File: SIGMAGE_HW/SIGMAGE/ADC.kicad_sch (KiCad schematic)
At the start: 34 parts, among them J2 SJ63073E, J3 SJ63073E, J4 SJ63073E, J5 SJ63073E, J7 TSW10607GS, J8 TSW10607GS, U4 OPA1612AIDRGR, U5 PCM1803ADB, U6 OPA1612AIDRGR, U7 PCM1803ADB

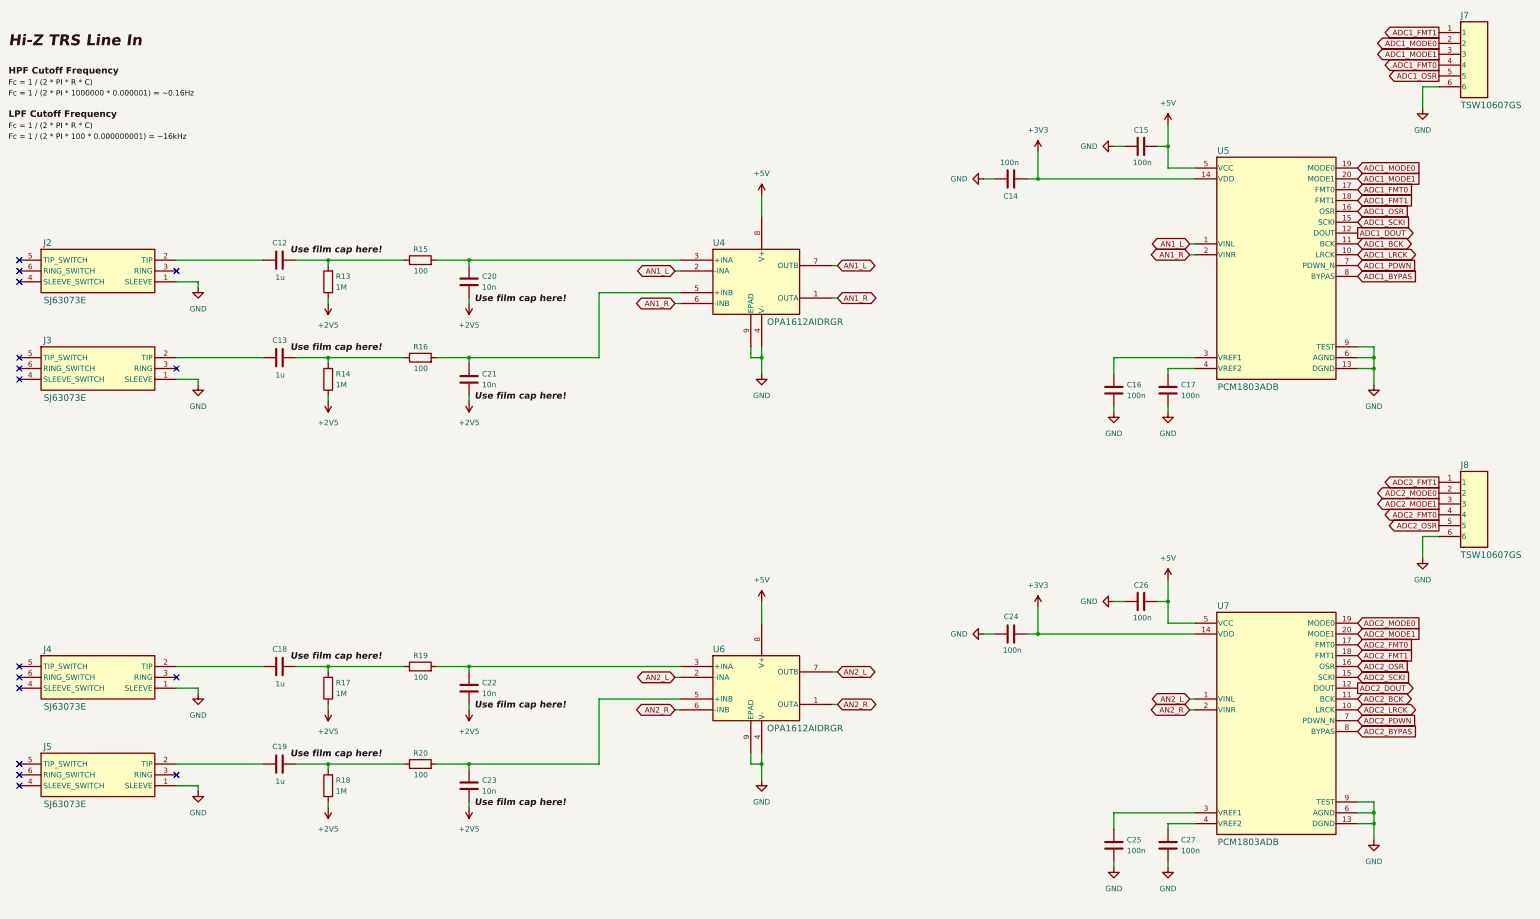
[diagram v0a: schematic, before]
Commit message: Adding a view DAC's
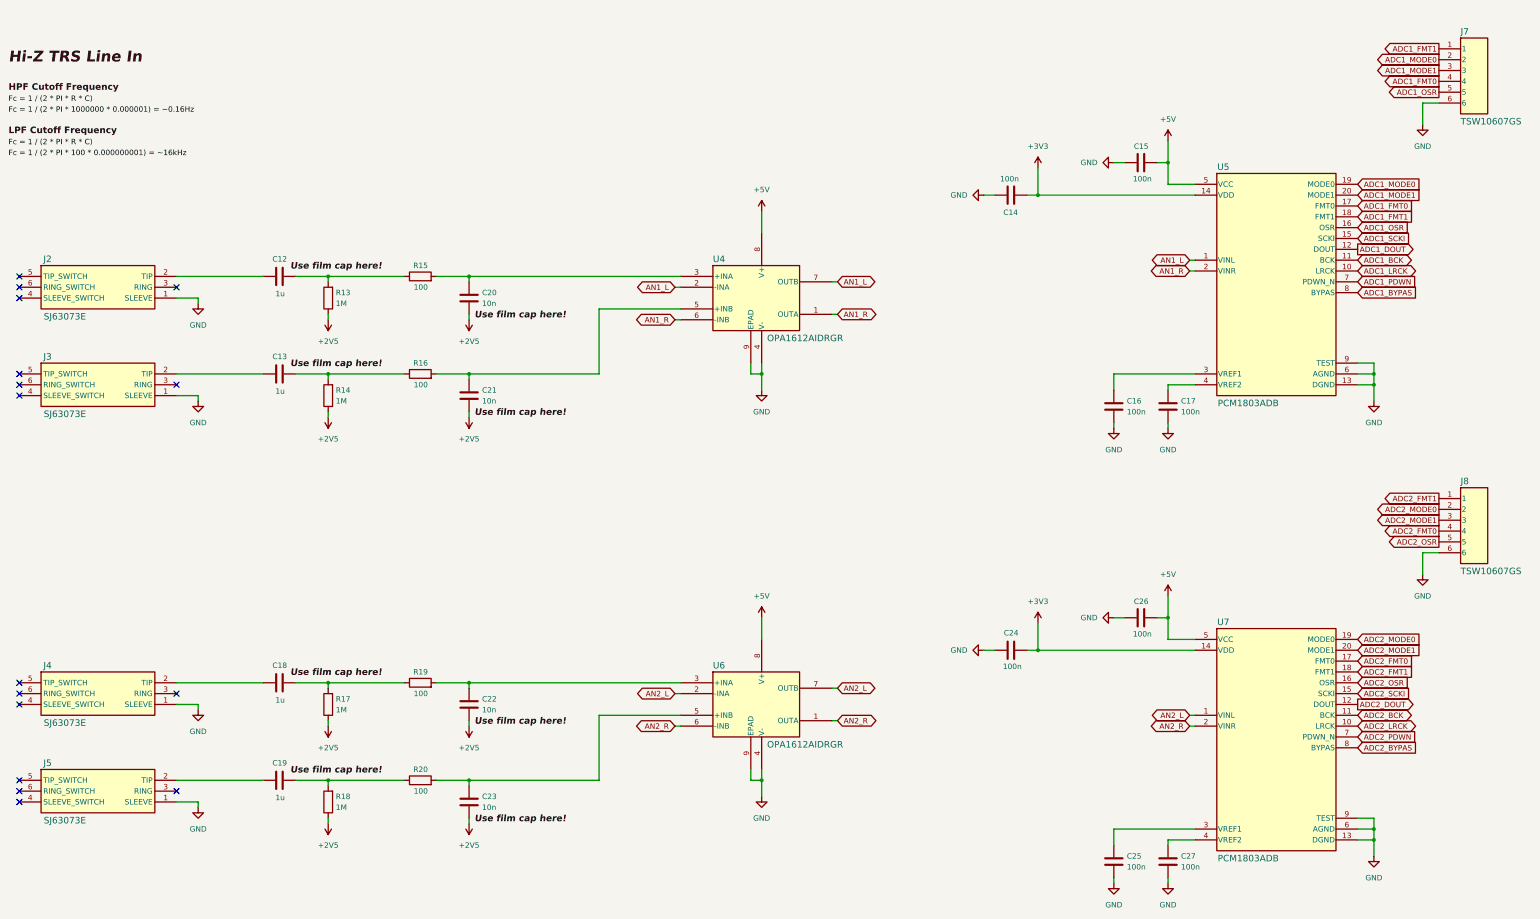
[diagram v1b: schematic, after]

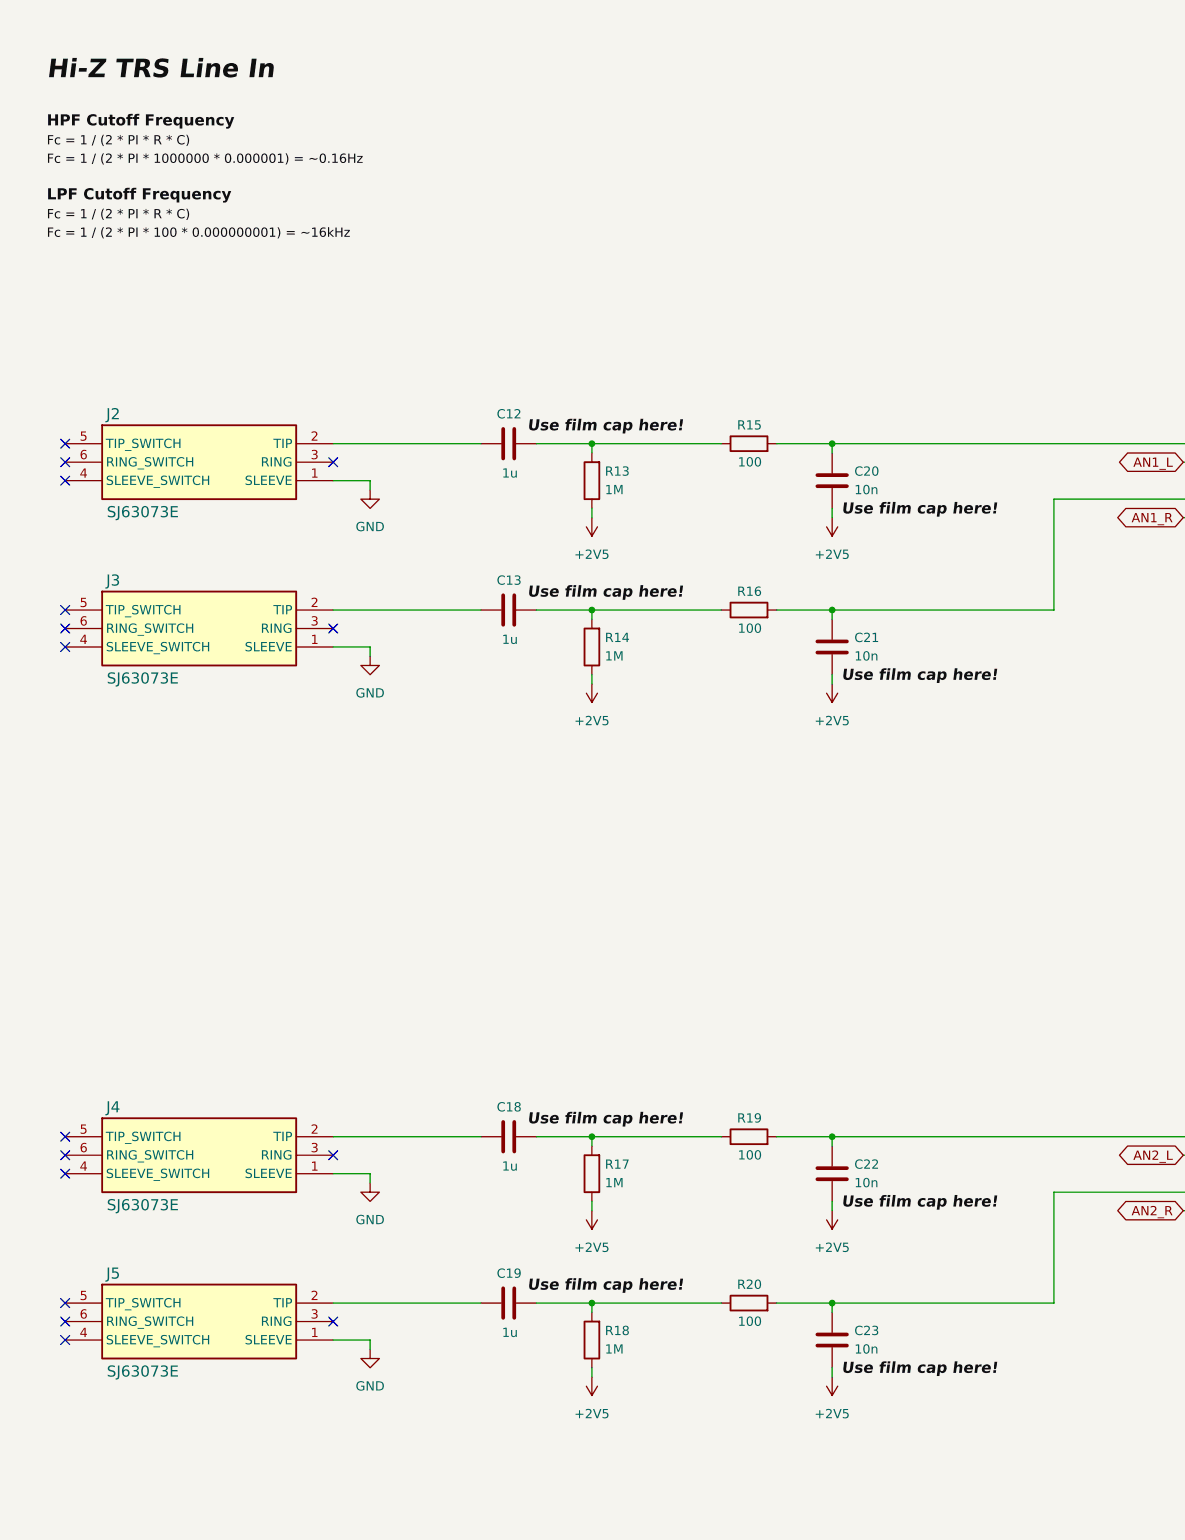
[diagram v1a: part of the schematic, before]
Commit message: More DAC changes
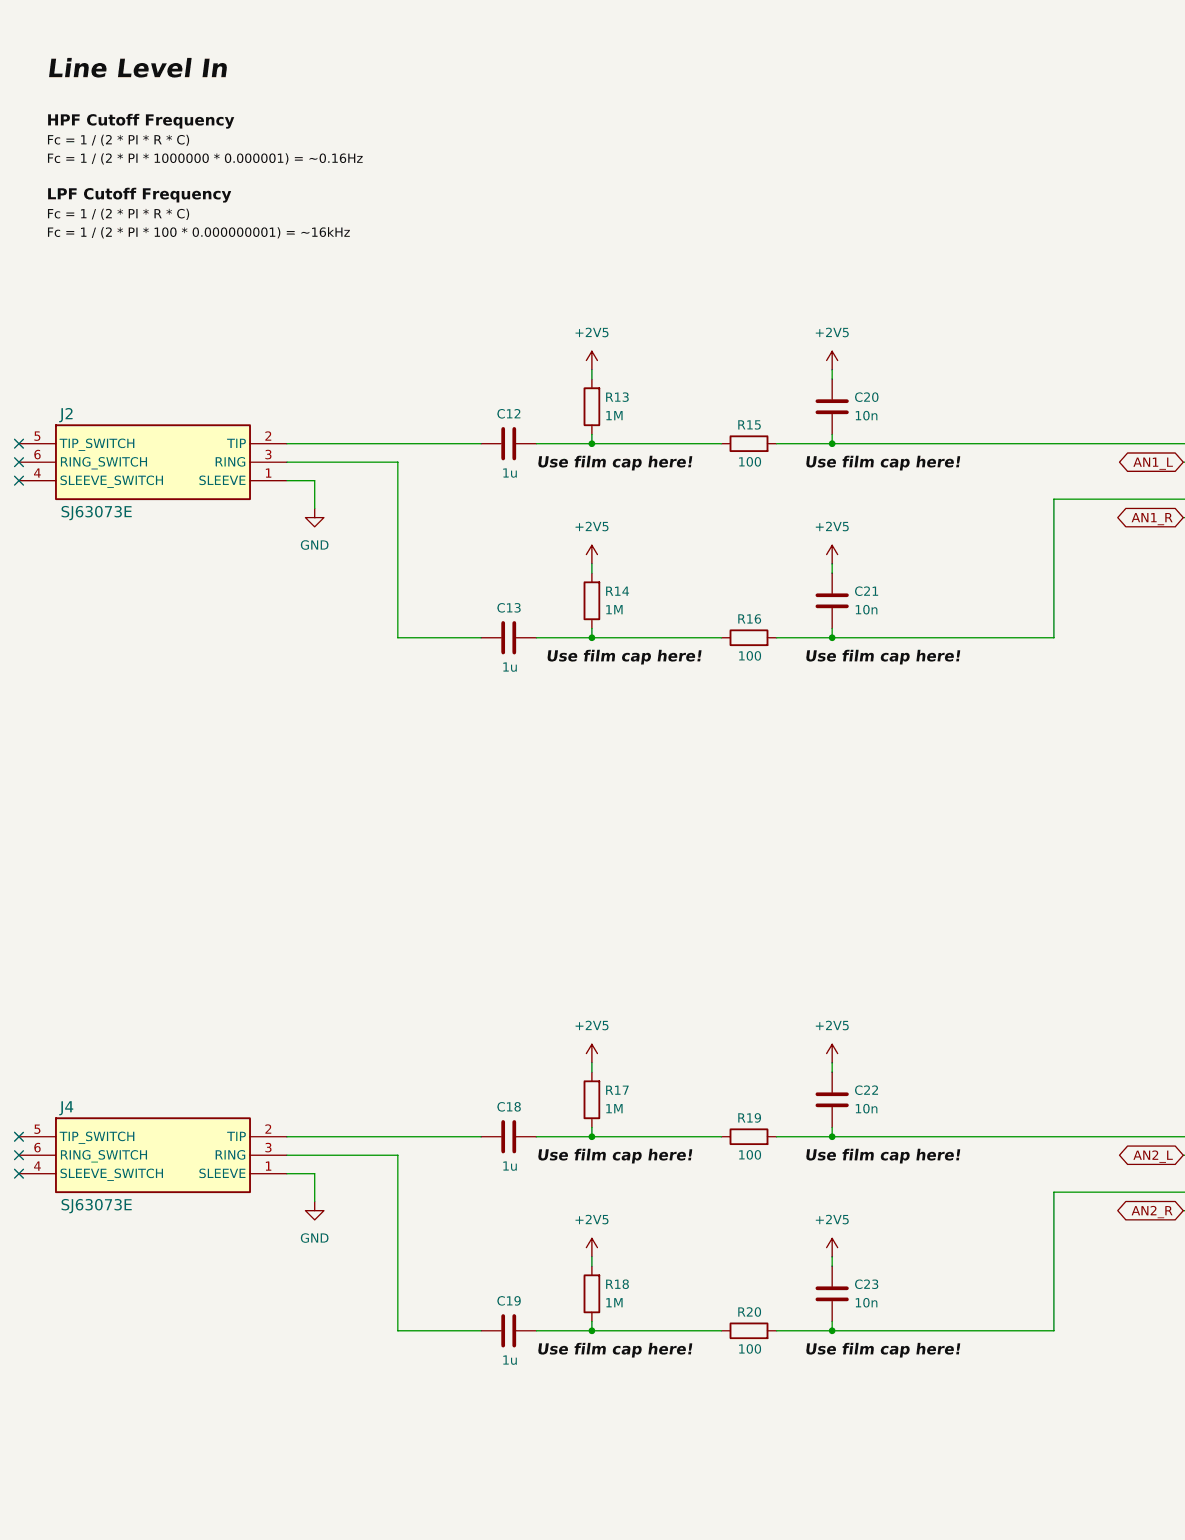
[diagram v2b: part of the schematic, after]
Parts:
- removed J3, J5: SJ63073E, SIGMAGE:SJ63073E, symbol SIGMAGE:SJ63073E
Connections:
- net +2V5: now also C20.1, C21.1, C22.1, C23.1, R13.2, R14.2, R17.2, R18.2; no longer C20.2, C21.2, C22.2, C23.2, R13.1, R14.1, R17.1, R18.1
- net at C13.1: now also J2.3 (RING)
- net at C18.2, R19.1: now also R17.1; no longer R17.2
- net at C19.1: now also J4.3 (RING)
- net at C19.2, R20.1: now also R18.1; no longer R18.2
- net at R15.2, U4.3 (+INA): now also C20.2; no longer C20.1
- net at C12.2, R15.1: now also R13.1; no longer R13.2
- net at R19.2, U6.3 (+INA): now also C22.2; no longer C22.1
- net at R16.2, U4.5 (+INB): now also C21.2; no longer C21.1
- net at C13.2, R16.1: now also R14.1; no longer R14.2
- net at R20.2, U6.5 (+INB): now also C23.2; no longer C23.1
- no-connect marks 16 -> 6
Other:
- moved on the sheet: C13, C19, J2, J4, R16, R20

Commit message: major changes
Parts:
- removed C14, C15: 100n, Capacitor_SMD:C_0603_1608Metric, symbol Device:C
- removed J7, J8: TSW10607GS, SIGMAGE:TSW10607GS, symbol SIGMAGE:TSW10607GS
- added C127, C128, C131, C132: 1u, Capacitor_SMD:C_1206_3216Metric, symbol Device:C
- added C129, C130, C133, C134: 10n, Capacitor_SMD:C_1206_3216Metric, symbol Device:C
- added C135, C136, C137, C138, C139, C140, C141, C142: 100n, Capacitor_SMD:C_1206_3216Metric, symbol Device:C
- added C143, C144: 100n, Capacitor_SMD:C_0603_1608Metric, symbol Device:C
- added J10, J11: SJ63073E, SIGMAGE:SJ63073E, symbol SIGMAGE:SJ63073E
- added R44, R45, R48, R49: 1M, Resistor_SMD:R_0603_1608Metric, symbol Device:R
- added R46, R47, R50, R51: 100, Resistor_SMD:R_0603_1608Metric, symbol Device:R
- added U16, U17: OPA1612AIDRGR, SIGMAGE:OPA1612AIDRGR, symbol SIGMAGE:OPA1612AIDRGR
- added U18, U19: PCM1803ADB, SIGMAGE:PCM1803ADB, symbol SIGMAGE:PCM1803ADB
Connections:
- net GND: now also C24.2, C26.2, C135.2, C136.2, C137.2, C138.2, C139.2, C140.2, C141.2, C142.2, C143.2, C144.2, J10.1 (SLEEVE), J11.1 (SLEEVE), U16.4 (V-), U16.9 (EPAD), U17.4 (V-), U17.9 (EPAD), U18.13 (DGND), U18.6 (AGND), U18.9 (TEST), U19.13 (DGND), U19.6 (AGND), U19.9 (TEST); no longer C24.1, C26.1
- net at C25.1: now also U7.4 (VREF2); no longer U7.3 (VREF1)
- net at C27.1: now also U19.3 (VREF1); no longer U7.4 (VREF2)
- net +2V5 renamed AVCC_2V5
- net AVCC_2V5: now also C129.1, C130.1, C133.1, C134.1, R44.2, R45.2, R48.2, R49.2
- net +3V3 renamed DVCC_3V3
- net DVCC_3V3: now also C135.1, C137.1, C139.1, C140.1, U18.14 (VDD), U19.14 (VDD); no longer C24.2
- net +5V renamed VCC_5V
- net VCC_5V: now also C136.1, C138.1, C141.1, C142.1, U16.8 (V+), U17.8 (V+), U18.5 (VCC), U19.5 (VCC); no longer C26.2
- new net: C130.2, R47.2, U16.5 (+INB)
- new net: C127.1, J10.2 (TIP)
- new net: C128.1, J10.3 (RING)
- new net: C144.1, U19.4 (VREF2)
- new net: C128.2, R45.1, R47.1
- new net: C131.2, R48.1, R50.1
- new net: C143.1, U18.4 (VREF2)
- new net: C127.2, R44.1, R46.1
- new net: C131.1, J11.2 (TIP)
- new net: C132.1, J11.3 (RING)
- new net: C134.2, R51.2, U17.5 (+INB)
- new net: C26.1, U18.3 (VREF1)
- new net: C132.2, R49.1, R51.1
- new net: C24.1, U7.3 (VREF1)
- new net: C129.2, R46.2, U16.3 (+INA)
- new net: C133.2, R50.2, U17.3 (+INA)
- new net ADC3_BCK: U18.11 (BCK)
- new net ADC3_BYPAS: U18.8 (BYPAS)
- new net ADC3_DOUT: U18.12 (DOUT)
- new net ADC3_FMT0: U18.17 (FMT0)
- new net ADC3_FMT1: U18.18 (FMT1)
- new net ADC3_LRCK: U18.10 (LRCK)
- new net ADC3_MODE0: U18.19 (MODE0)
- new net ADC3_MODE1: U18.20 (MODE1)
- new net ADC3_OSR: U18.16 (OSR)
- new net ADC3_PDWN: U18.7 (PDWN_N)
- new net ADC3_SCKI: U18.15 (SCKI)
- new net ADC4_BCK: U19.11 (BCK)
- new net ADC4_BYPAS: U19.8 (BYPAS)
- new net ADC4_DOUT: U19.12 (DOUT)
- new net ADC4_FMT0: U19.17 (FMT0)
- new net ADC4_FMT1: U19.18 (FMT1)
- new net ADC4_LRCK: U19.10 (LRCK)
- new net ADC4_MODE0: U19.19 (MODE0)
- new net ADC4_MODE1: U19.20 (MODE1)
- new net ADC4_OSR: U19.16 (OSR)
- new net ADC4_PDWN: U19.7 (PDWN_N)
- new net ADC4_SCKI: U19.15 (SCKI)
- new net AN3_L: U16.2 (-INA), U16.7 (OUTB), U18.1 (VINL)
- new net AN3_R: U16.1 (OUTA), U16.6 (-INB), U18.2 (VINR)
- new net AN4_L: U17.2 (-INA), U17.7 (OUTB), U19.1 (VINL)
- new net AN4_R: U17.1 (OUTA), U17.6 (-INB), U19.2 (VINR)
- no-connect marks 6 -> 12
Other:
- moved on the sheet: C12, C13, C16, C17, C18, C19, C20, C21, C22, C23, J2, J4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

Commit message: changes
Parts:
- C129, C130, C133, C134, C20, C21, C22, C23: value 10n -> 1n
- R15, R16, R19, R20, R46, R47, R50, R51: value 100 -> 6500
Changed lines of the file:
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@@
 		)
 	)
-	(label "Adjust filters up to 25kHz"
-		(at 92.71 30.48 0)
-		(effects
-			(font
-				(size 3.81 3.81)
-				(thickness 0.508)
-				(bold yes)
-				(italic yes)
-				(color 255 0 0 1)
-			)
-			(justify left bottom)
-		)
-	)
 	(label "ADC1_BCK"
 		(at 384.81 36.83 180)
@@
 		)
 	)
-	(label "Fc = 1 {slash} (2 * PI * 100 * 0.000000001) = ~16kHz"
+	(label "Fc = 1 {slash} (2 * PI * 6500 * 0.000000001) = ~25kHz"
 		(at 17.78 43.18 0)
 		(effects
@@
 			)
 		)
-		(property "Value" "10n"
+		(property "Value" "1n"
 			(at 144.018 204.47 0)
 			(show_name no)
@@
 			)
 		)
-		(property "Value" "100"
-			(at 131.318 210.82 90)
+		(property "Value" "6500"
+			(at 132.08 210.82 90)
 			(show_name no)
 			(do_not_autoplace no)
@@
 			)
 		)
-		(property "Value" "100"
-			(at 131.318 59.69 90)
+		(property "Value" "6500"
+			(at 132.08 59.69 90)
 			(show_name no)
 			(do_not_autoplace no)
@@
 			)
 		)
-		(property "Value" "10n"
+		(property "Value" "1n"
 			(at 144.018 53.34 0)
 			(show_name no)
@@
 			)
 		)
-		(property "Value" "100"
-			(at 131.318 86.36 90)
+		(property "Value" "6500"
+			(at 132.08 86.36 90)
 			(show_name no)
 			(do_not_autoplace no)
@@
 			)
 		)
-		(property "Value" "10n"
+		(property "Value" "1n"
 			(at 144.018 115.57 0)
 			(show_name no)
@@
 			)
 		)
-		(property "Value" "10n"
+		(property "Value" "1n"
 			(at 144.018 142.24 0)
 			(show_name no)
@@
 			)
 		)
-		(property "Value" "10n"
+		(property "Value" "1n"
 			(at 144.018 267.97 0)
 			(show_name no)
@@
 			)
 		)
-		(property "Value" "100"
-			(at 131.318 121.92 90)
+		(property "Value" "6500"
+			(at 132.08 121.92 90)
 			(show_name no)
 			(do_not_autoplace no)
@@
 			)
 		)
-		(property "Value" "10n"
+		(property "Value" "1n"
 			(at 144.018 177.8 0)
 			(show_name no)
@@
 			)
 		)
-		(property "Value" "100"
-			(at 131.318 148.59 90)
+		(property "Value" "6500"
+			(at 132.08 148.59 90)
 			(show_name no)
 			(do_not_autoplace no)
@@
 			)
 		)
-		(property "Value" "100"
-			(at 131.318 247.65 90)
+		(property "Value" "6500"
+			(at 132.08 247.65 90)
 			(show_name no)
 			(do_not_autoplace no)
@@
 			)
 		)
-		(property "Value" "10n"
+		(property "Value" "1n"
 			(at 144.018 241.3 0)
 			(show_name no)
@@
 			)
 		)
-		(property "Value" "100"
-			(at 131.318 184.15 90)
+		(property "Value" "6500"
+			(at 132.08 184.15 90)
 			(show_name no)
 			(do_not_autoplace no)
@@
 			)
 		)
-		(property "Value" "100"
-			(at 131.318 274.32 90)
+		(property "Value" "6500"
+			(at 132.08 274.32 90)
 			(show_name no)
 			(do_not_autoplace no)
@@
 			)
 		)
-		(property "Value" "10n"
+		(property "Value" "1n"
 			(at 144.018 80.01 0)
 			(show_name no)

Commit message: finishing up
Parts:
- removed C143, C144, C16, C17, C24, C25, C26, C27: 100n, Capacitor_SMD:C_0603_1608Metric, symbol Device:C
- added C125, C173, C175, C179, C180, C181, C182, C183, C184, C185, C186, C89: 100n, Capacitor_SMD:C_1206_3216Metric, symbol Device:C
- added C126, C174, C176, C90: 10u, Capacitor_SMD:C_1206_3216Metric, symbol Device:C
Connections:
- net GND: now also C125.2, C126.2, C173.2, C174.2, C175.2, C176.2, C179.2, C180.2, C181.2, C182.2, C183.2, C184.2, C185.2, C186.2, C89.2, C90.2
- net VCC_5V: now also C125.1, C126.1, C173.1, C174.1, C175.1, C176.1, C89.1, C90.1
- net at U5.3 (VREF1): now also C179.1
- net at U5.4 (VREF2): now also C180.1
- net at U19.4 (VREF2): now also C186.1
- net at U19.3 (VREF1): now also C185.1
- net at U7.4 (VREF2): now also C182.1
- net at U18.4 (VREF2): now also C184.1
- net at U18.3 (VREF1): now also C183.1
- net at U7.3 (VREF1): now also C181.1
- net AN1_L renamed AN_IN1_L
- net AN1_R renamed AN_IN1_R
- net AN2_L renamed AN_IN2_L
- net AN2_R renamed AN_IN2_R
- net AN3_L renamed AN_IN3_L
- net AN3_R renamed AN_IN3_R
- net AN4_L renamed AN_IN4_L
- net AN4_R renamed AN_IN4_R
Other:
- moved on the sheet: C12, C127, C128, C129, C13, C130, C131, C132, C133, C134, C135, C136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

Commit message: almost done
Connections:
- net VCC_5V renamed AVCC_5V
